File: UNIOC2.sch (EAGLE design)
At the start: 1 part, among them IC1 XMEGA128A1

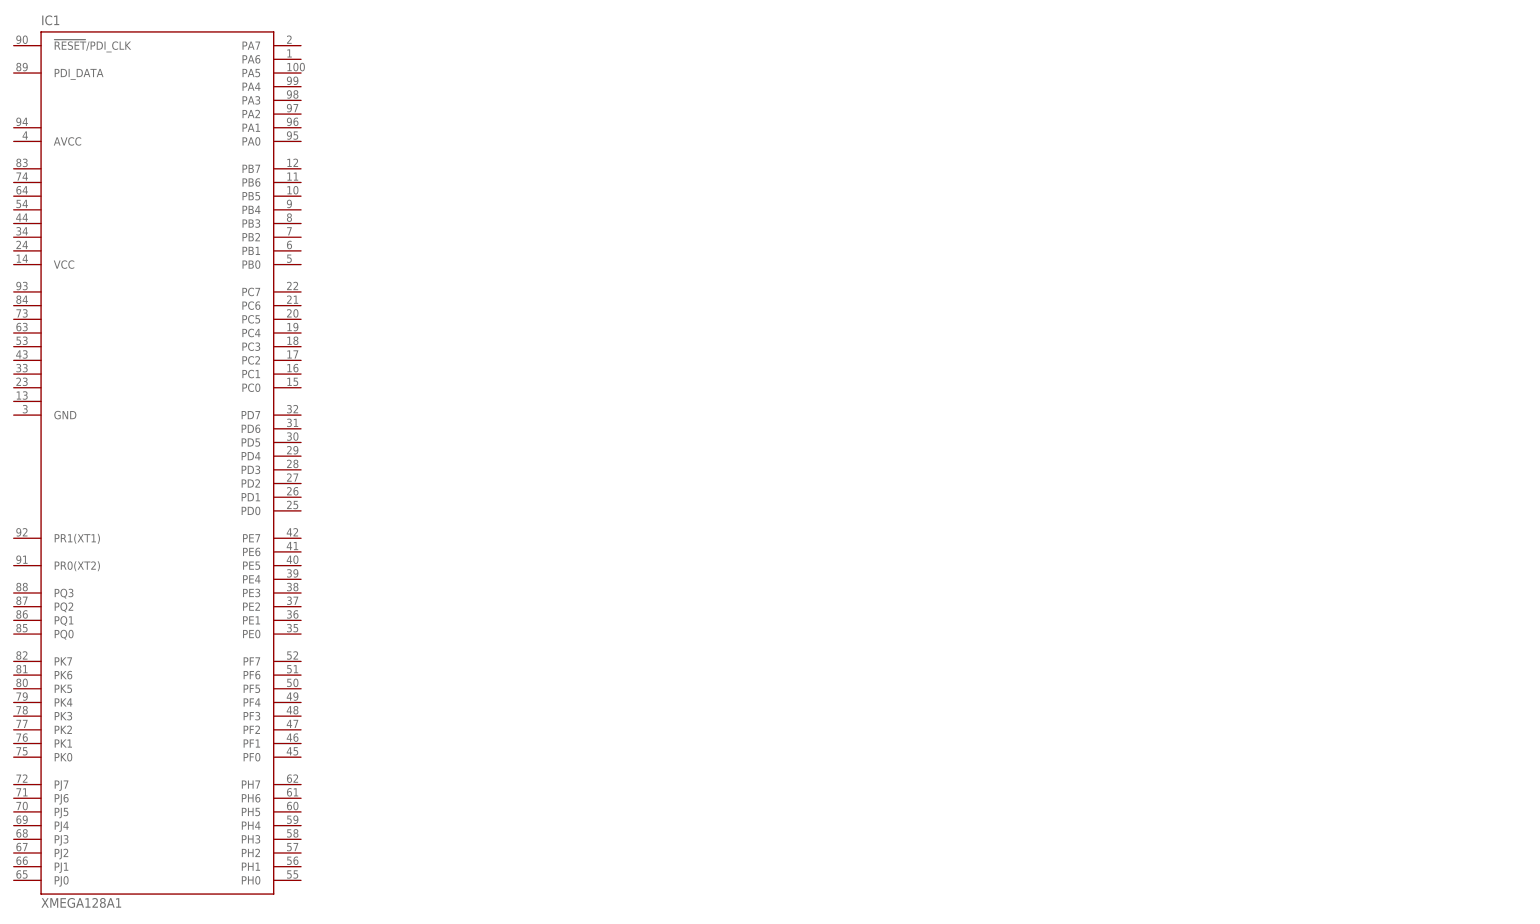
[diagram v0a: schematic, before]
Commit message: Ajout du FPGA de robotter.
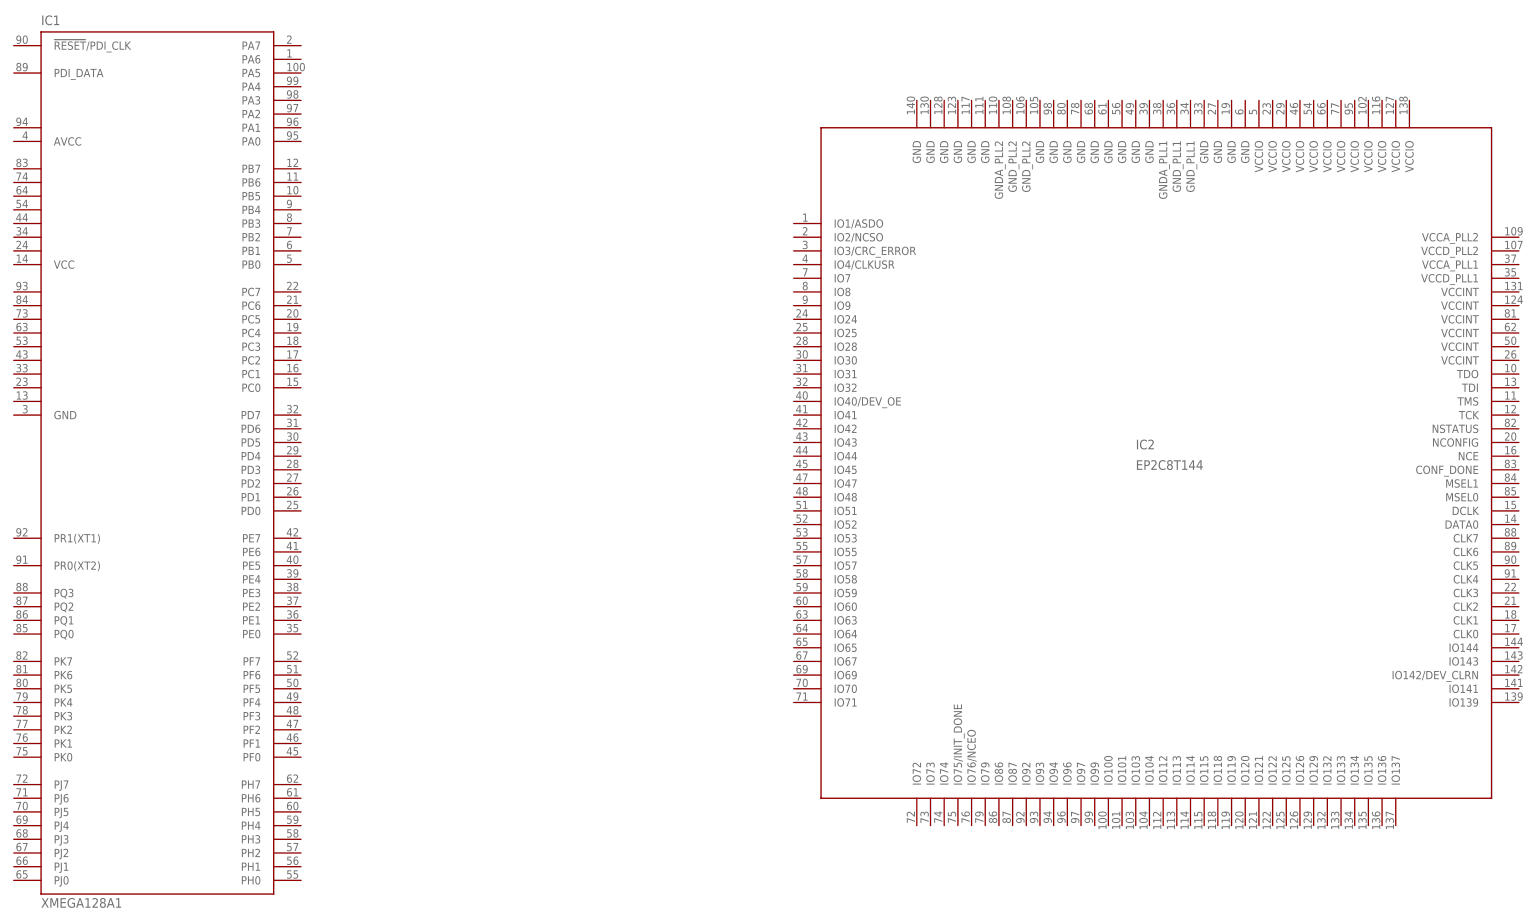
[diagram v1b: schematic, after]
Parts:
- added IC2: EP2C8T144, robotter_ic:EP2C8T144
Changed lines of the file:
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@@
 <layer number="51" name="tDocu" color="6" fill="9" visible="no" active="no"/>
 <layer number="52" name="bDocu" color="7" fill="1" visible="no" active="no"/>
+<layer number="53" name="tGND_GNDA" color="7" fill="9" visible="no" active="no"/>
+<layer number="54" name="bGND_GNDA" color="1" fill="9" visible="no" active="no"/>
 <layer number="91" name="Nets" color="2" fill="1" visible="yes" active="yes"/>
 <layer number="92" name="Busses" color="1" fill="1" visible="yes" active="yes"/>
@@
 <layer number="97" name="Info" color="7" fill="1" visible="yes" active="yes"/>
 <layer number="98" name="Guide" color="6" fill="1" visible="yes" active="yes"/>
+<layer number="101" name="Hidden" color="15" fill="1" visible="yes" active="yes"/>
+<layer number="102" name="Changes" color="12" fill="1" visible="yes" active="yes"/>
+<layer number="144" name="Drill_legend" color="7" fill="1" visible="yes" active="yes"/>
 </layers>
 <schematic xreflabel="%F%N/%S.%C%R" xrefpart="/%S.%C%R">
@@
 <parts>
 <part name="IC1" library="atmel" deviceset="XMEGA128A1" device=""/>
+<part name="IC2" library="robotter_ic" deviceset="EP2C8T144" device=""/>
 </parts>
 <sheets>
@@
 <instances>
 <instance part="IC1" gate="G$1" x="-40.64" y="25.4"/>
+<instance part="IC2" gate="G$1" x="147.32" y="25.4"/>
 </instances>
 <busses>
